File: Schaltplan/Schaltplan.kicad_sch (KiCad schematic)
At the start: 15 parts, among them P1 USB_C_Plug_USB2.0, P2 USB_C_Plug_USB2.0, P3 USB_C_Plug_USB2.0, U1 ACS712xLCTR-05B, U2 LM2596S, U3 DS18B20, U4 DS18B20, U5 LM2596S, U6 DS3502, U7 DS3502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

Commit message: Weird Stuff hapened
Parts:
- removed BT3: Battery_Cell, symbol Device:Battery_Cell
- removed P3: USB_C_Plug_USB2.0, symbol Connector:USB_C_Plug_USB2.0
- removed U1: ACS712xLCTR-05B, Package_SO:SOIC-8_3.9x4.9mm_P1.27mm, symbol Sensor_Current:ACS712xLCTR-05B
- added BT2: Battery_Cell, symbol Device:Battery_Cell
- added U1: LM2596S, Package_TO_SOT_SMD:TO-263-5_TabPin3, symbol Regulator_Switching:LM2596S-5
- U8: value LM2596S -> ACS712
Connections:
- net at U8.2 (Rechts): now also BT1.2 (-), U2.5 (IN-)
- net at A1.4 (GND), U3.1 (GND), U4.1 (GND)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: now also U8.4 (Links), U8.5 (GND); no longer U2.3 (GND), U8.3 (GND)
- net at U6.6 (RH): now also U1.6 (R1); no longer U8.6 (R1)
- net at U6.7 (RW): now also U1.7 (R2); no longer U8.7 (R2)
- net at U6.8 (RL): now also U1.8 (R3); no longer U8.8 (R3)
- net at BT1.1 (+): now also U2.1 (IN+), BT2.2 (-), U1.5 (IN-)
- net at A1.27 (+5V), U3.3 (V_{DD}), U4.3 (V_{DD})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: now also U8.1 (OUT)
- net at U5.1 (IN+): now also P1.S1 (+), U1.4 (OUT+)
- net at U5.2 (OUT-): now also P2.A1 (-), P2.A4 (Shield)
- net at U5.4 (OUT+): now also P2.S1 (+)
- net at U5.5 (IN-): now also P1.A1 (-), U2.2 (OUT-)
- net at R1.1: now also A1.5 (D2)
- net at R1.2: now also BT2.1 (+), U1.1 (IN+)
- net at U2.4 (OUT+): now also U1.2 (OUT-)
- net at P1.A12 (GND), P1.B1 (GND), P1.B12 (GND): no longer P1.A1 (GND)
- net at P1.A9 (VBUS), P1.B4 (VBUS), P1.B9 (VBUS): no longer P1.A4 (VBUS)
- net at P2.A12 (GND), P2.B1 (GND), P2.B12 (GND): no longer P2.A1 (GND)
- net at P2.A9 (VBUS), P2.B4 (VBUS), P2.B9 (VBUS): no longer P2.A4 (VBUS)
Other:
- note removed: "IN+"
- note removed: "OUT+"
- moved on the sheet: A1, BT1, U4, U6, U7

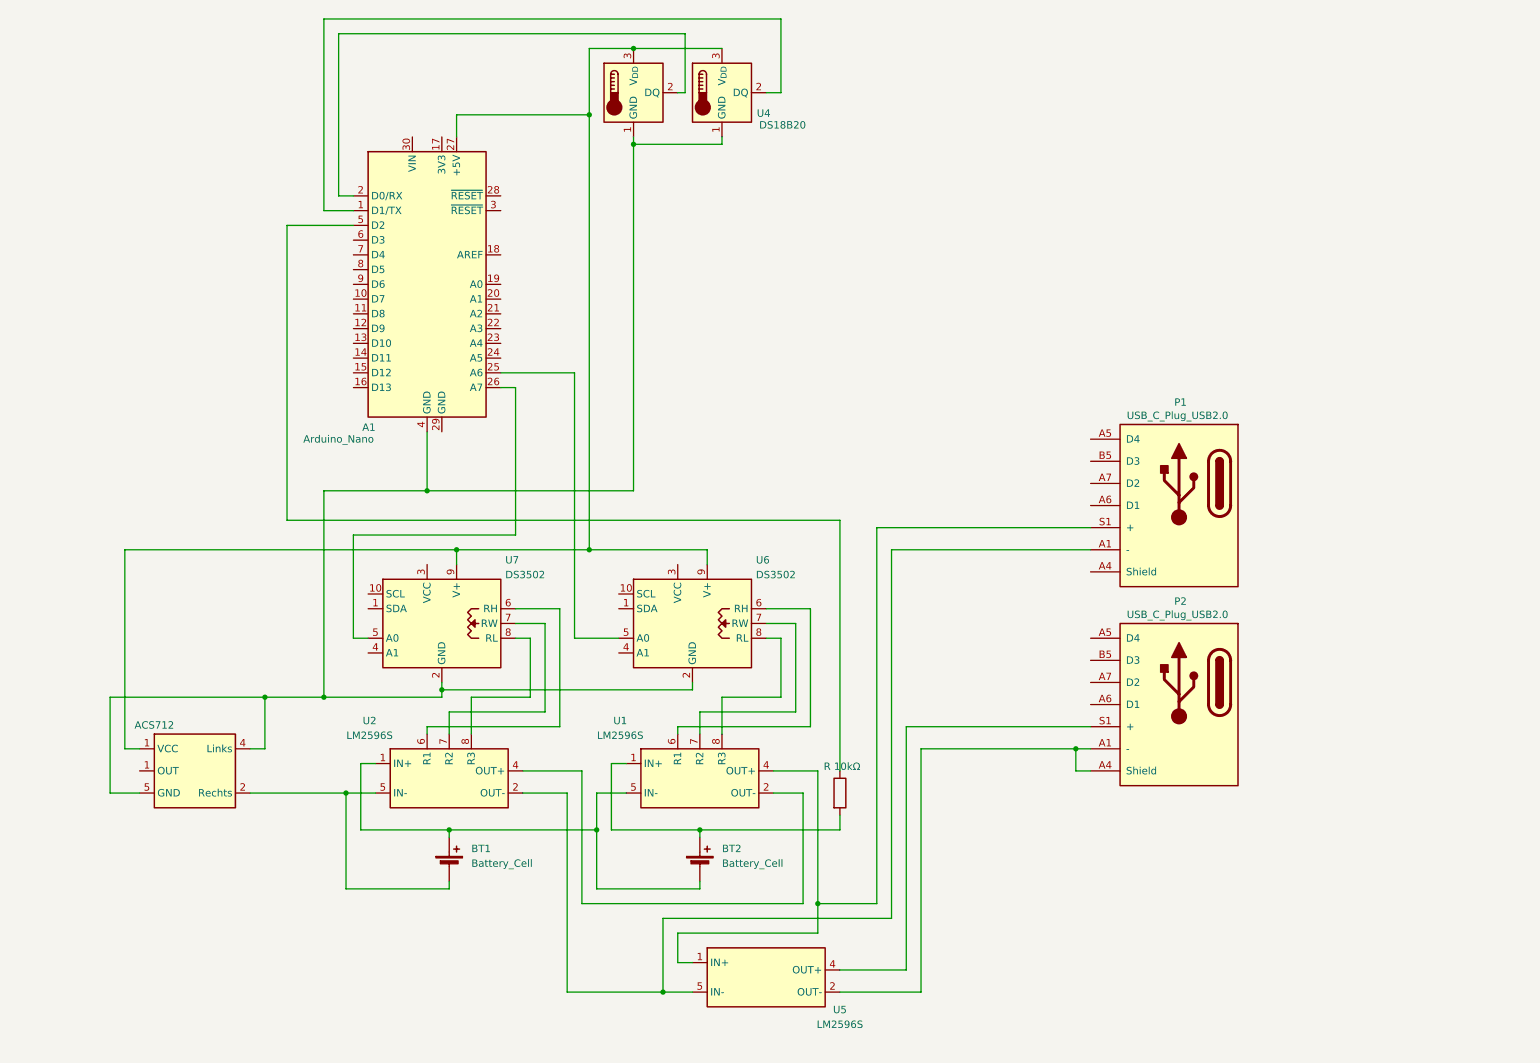
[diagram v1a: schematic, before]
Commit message: Add USB-C Plug connector properties and update layout in Schaltplan
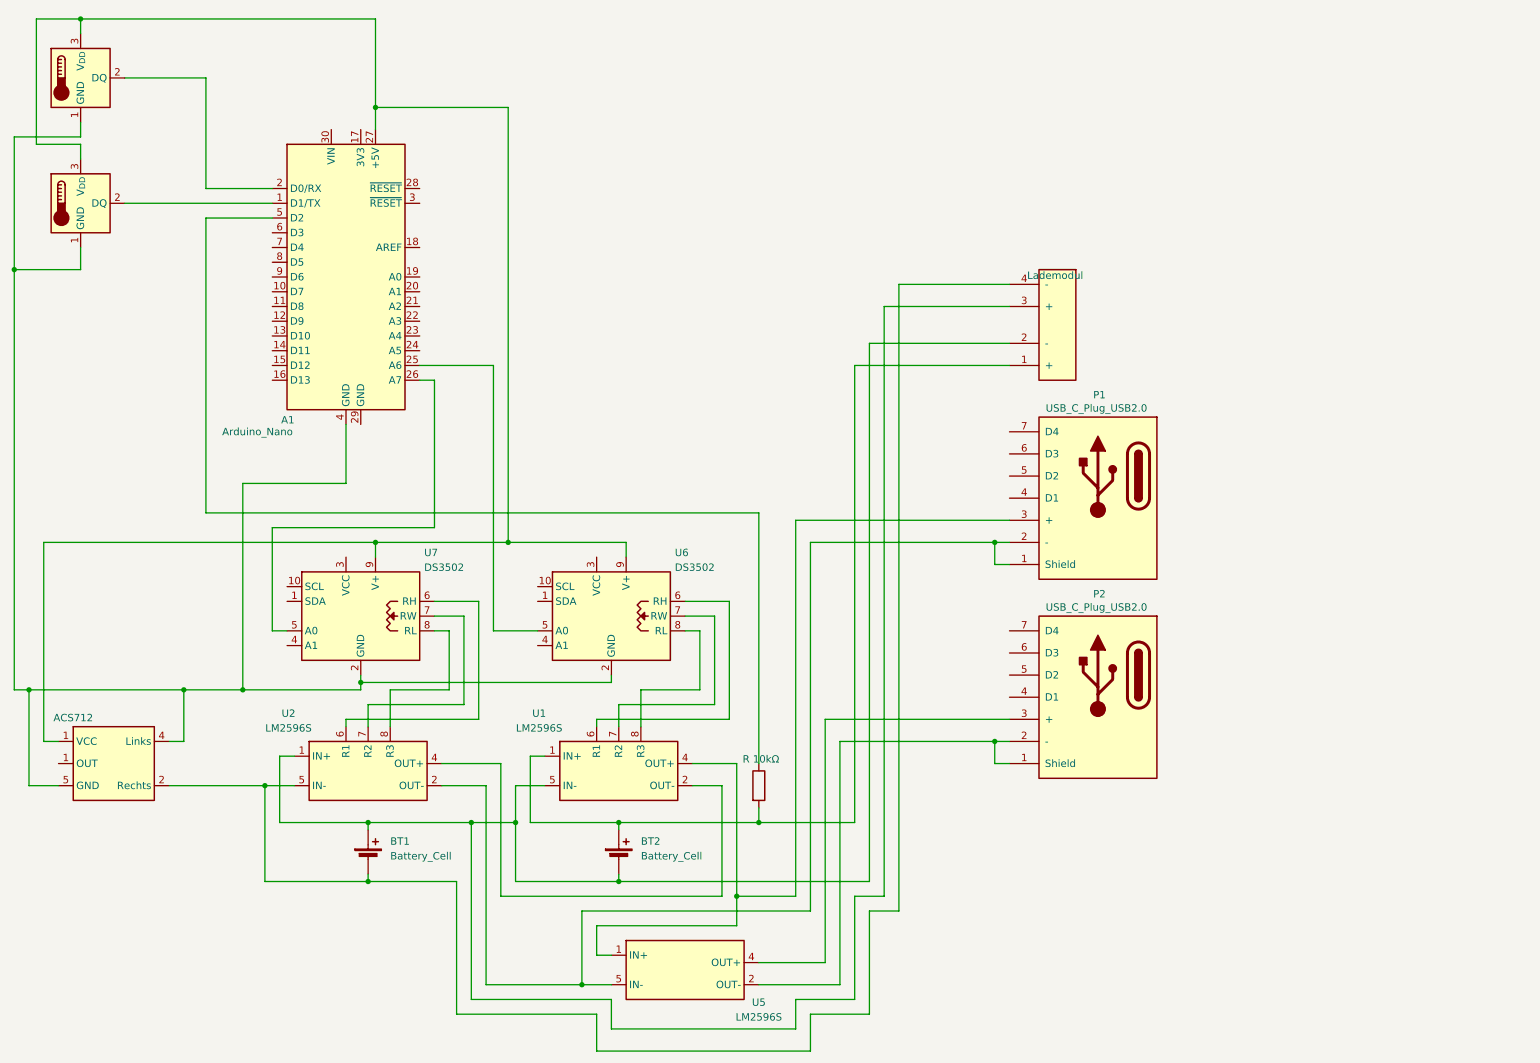
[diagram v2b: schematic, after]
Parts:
- removed U4: DS18B20, Package_TO_SOT_THT:TO-92_Inline, symbol Sensor_Temperature:DS18B20
- added P3: Lademodul, symbol Connector:USB_C_Plug_USB2.0
- added U9: DS18B20, Package_TO_SOT_THT:TO-92_Inline, symbol Sensor_Temperature:DS18B20
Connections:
- net at BT1.1 (+), BT2.2 (-), U1.5 (IN-)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: now also P3.2 (-), P3.3 (+)
- net at BT1.2 (-), U2.5 (IN-), U8.2 (Rechts): now also P3.4 (-)
- net at U2.2 (OUT-), U5.5 (IN-): now also P1.1 (Shield), P1.2 (-); no longer P1.A1 (-)
- net at U1.4 (OUT+), U5.1 (IN+): now also P1.3 (+); no longer P1.S1 (+)
- net at A1.4 (GND), U3.1 (GND), U6.2 (GND)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: now also U9.1 (GND)
- net at U3.2 (DQ): now also A1.1 (D1/TX); no longer A1.2 (D0/RX)
- net at A1.27 (+5V), U3.3 (V_{DD}), U6.9 (V+)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: now also U9.3 (V_{DD})
- net at BT2.1 (+), R1.2, U1.1 (IN+): now also P3.1 (+)
- net at U5.4 (OUT+): now also P2.3 (+); no longer P2.S1 (+)
- new net: P3.A12 (GND), P3.B1 (GND), P3.B12 (GND)
- new net: P3.A9 (VBUS), P3.B4 (VBUS), P3.B9 (VBUS)
- new net: A1.2 (D0/RX), U9.2 (DQ)
- new net: P2.1 (Shield), P2.2 (-), U5.2 (OUT-)
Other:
- moved on the sheet: A1, BT1, BT2, P2, U1, U2, U5, U6, U7

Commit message: Update Schaltplan title and component values for clarity and accuracy
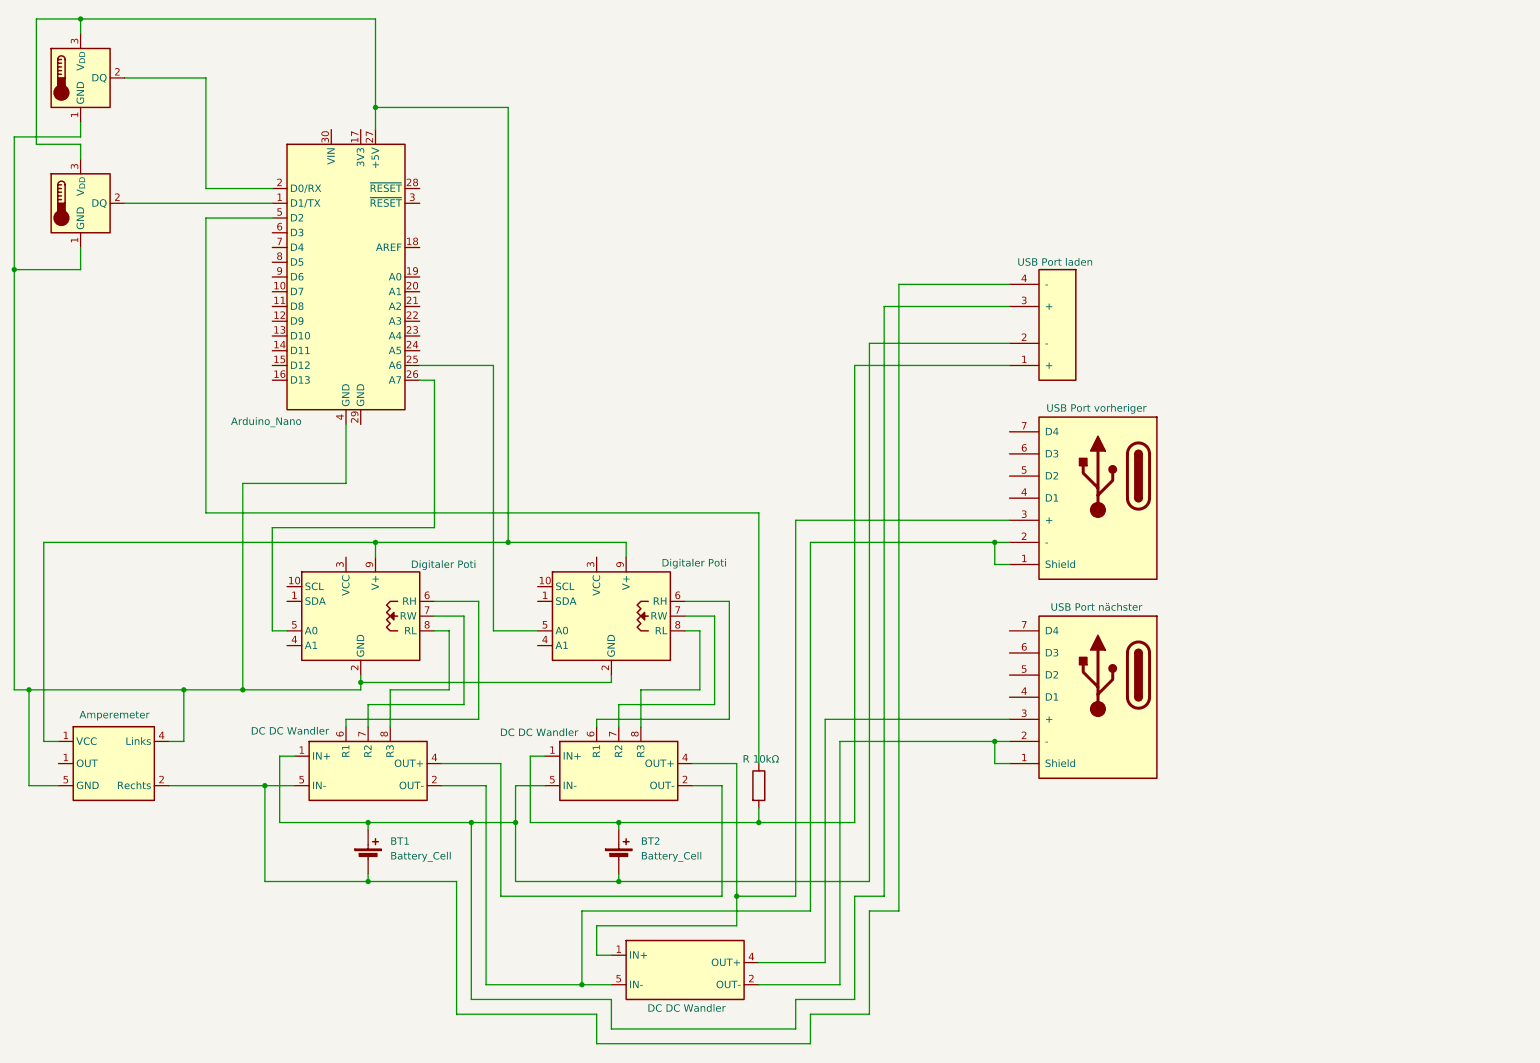
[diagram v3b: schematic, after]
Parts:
- P1: value USB_C_Plug_USB2.0 -> USB Port vorheriger
- P2: value USB_C_Plug_USB2.0 -> USB Port nächster
- P3: value Lademodul -> USB Port laden
- U1, U2, U5: value LM2596S -> DC DC Wandler
- U6, U7: value DS3502 -> Digitaler Poti
- U8: value ACS712 -> Amperemeter
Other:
- company: AkkuCraft -> Akku-Craft
- title: Schaltplan Powerbank -> Akku-Craft Modul
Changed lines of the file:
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@@
 	(paper "A4")
 	(title_block
-		(title "Schaltplan Powerbank")
-		(date "2026-01-15")
-		(company "AkkuCraft")
+		(title "Akku-Craft Modul")
+		(date "2026-03-10")
+		(company "Akku-Craft")
 	)
 	(junction
@@
 	(wire
 		(pts
-			(xy 118.11 193.04) (xy 154.94 193.04)
+			(xy 118.11 191.77) (xy 154.94 191.77)
 		)
 		(stroke
@@
 	(wire
 		(pts
-			(xy 154.94 193.04) (xy 154.94 186.69)
+			(xy 154.94 191.77) (xy 154.94 186.69)
 		)
 		(stroke
@@
 	(wire
 		(pts
-			(xy 118.11 186.69) (xy 118.11 193.04)
+			(xy 118.11 186.69) (xy 118.11 191.77)
 		)
 		(stroke
@@
 			)
 		)
-		(property "Value" "Lademodul"
-			(at 197.104 59.436 0)
+		(property "Value" "USB Port laden"
+			(at 197.104 57.15 0)
 			(effects
 				(font
@@
 		(on_board yes)
 		(dnp no)
-		(fields_autoplaced yes)
 		(property "Reference" "U2"
-			(at 65.024 134.874 0)
-			(effects
-				(font
-					(size 1.27 1.27)
-				)
-			)
-		)
-		(property "Value" "LM2596S"
-			(at 65.024 137.414 0)
+			(at 78.74 152.4 0)
+			(effects
+				(font
+					(size 1.27 1.27)
+				)
+				(hide yes)
+			)
+		)
+		(property "Value" "DC DC Wandler"
+			(at 65.278 137.922 0)
 			(effects
 				(font
@@
 				)
 				(justify left)
-			)
-		)
-		(property "Value" "DS3502"
-			(at 88.392 109.728 0)
+				(hide yes)
+			)
+		)
+		(property "Value" "Digitaler Poti"
+			(at 86.106 109.22 0)
 			(effects
 				(font
@@
 	)
 	(symbol
-		(lib_name "USB_C_Plug_USB2.0_2")
+		(lib_name "USB_C_Plug_USB2.0_3")
 		(lib_id "Connector:USB_C_Plug_USB2.0")
 		(at 204.47 93.98 0)
@@
 					(size 1.27 1.27)
 				)
-			)
-		)
-		(property "Value" "USB_C_Plug_USB2.0"
+				(hide yes)
+			)
+		)
+		(property "Value" "USB Port vorheriger"
 			(at 204.216 82.296 0)
 			(effects
@@
 					(size 1.27 1.27)
 				)
-			)
-		)
-		(property "Value" "LM2596S"
-			(at 146.05 187.198 0)
+				(hide yes)
+			)
+		)
+		(property "Value" "DC DC Wandler"
+			(at 133.604 185.674 0)
 			(effects
 				(font
@@
 				)
 				(justify left)
-			)
-		)
-		(property "Value" "DS3502"
-			(at 131.572 109.728 0)
+				(hide yes)
+			)
+		)
+		(property "Value" "Digitaler Poti"
+			(at 129.286 108.966 0)
 			(effects
 				(font
@@
 		(on_board yes)
 		(dnp no)
-		(fields_autoplaced yes)
 		(property "Reference" "U1"
-			(at 108.204 134.874 0)
-			(effects
-				(font
-					(size 1.27 1.27)
-				)
-			)
-		)
-		(property "Value" "LM2596S"
-			(at 108.204 137.414 0)
+			(at 121.92 152.4 0)
+			(effects
+				(font
+					(size 1.27 1.27)
+				)
+				(hide yes)
+			)
+		)
+		(property "Value" "DC DC Wandler"
+			(at 108.204 138.176 0)
 			(effects
 				(font
@@
 					(size 1.27 1.27)
 				)
-			)
-		)
-		(property "Value" "USB_C_Plug_USB2.0"
+				(hide yes)
+			)
+		)
+		(property "Value" "USB Port nächster"
 			(at 204.216 116.586 0)
 			(effects
@@
 				)
 				(justify left)
+				(hide yes)
 			)
 		)
 		(property "Value" "Arduino_Nano"
-			(at 53.594 86.36 0)
+			(at 55.118 84.582 0)
 			(effects
 				(font
@@
 			)
 		)
-		(property "Value" "ACS712"
-			(at 27.94 135.636 0)
-			(effects
-				(font
+		(property "Value" "Amperemeter"
+			(at 35.052 135.128 0)
+			(effects
+				(font
